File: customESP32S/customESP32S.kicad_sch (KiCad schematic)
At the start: 0 parts

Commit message: finished two USB micro connections with their protection circuit
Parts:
- added C1, C2: 10uF/25V, symbol Device:C_Small
- added D1, D8: 1N5819, Diode_THT:D_DO-41_SOD81_P10.16mm_Horizontal, symbol Diode:1N5819
- added D2, D3, D4, D5, D6, D7: SD05_SOD323, Diode_SMD:D_SOD-323, symbol Diode:SD05_SOD323
- added J1, J2: USB_B_Micro, symbol Connector:USB_B_Micro
- added U1: RT9193-33GB, RT9193-33GB:SOT94P279X129-5N, symbol RT9193-33GB:RT9193-33GB
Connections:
- new net GND: C1.1, C2.1, D2.1 (A1), D3.1 (A1), D4.1 (A1), D5.1 (A1), D6.1 (A1), D7.1 (A1), J1.5 (GND), J1.6 (Shield), J2.5 (GND), J2.6 (Shield)
- new net GPIO19: D2.2 (A2), J1.2 (D-)
- new net GPIO20: D3.2 (A2), J1.3 (D+)
- new net USB_DN: D5.2 (A2), J2.2 (D-)
- new net USB_DP: D6.2 (A2), J2.3 (D+)
- new net VBUS: D7.2 (A2), D8.2 (A), J2.1 (VBUS)
- new net VBUSB: D1.2 (A), D4.2 (A2), J1.1 (VBUS)
- new net VCC_5V: C1.2, C2.2, D1.1 (K), D8.1 (K)
- no-connect marks 0 -> 2
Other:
- note added: "ESP USB"
- note added: "USB to UART"

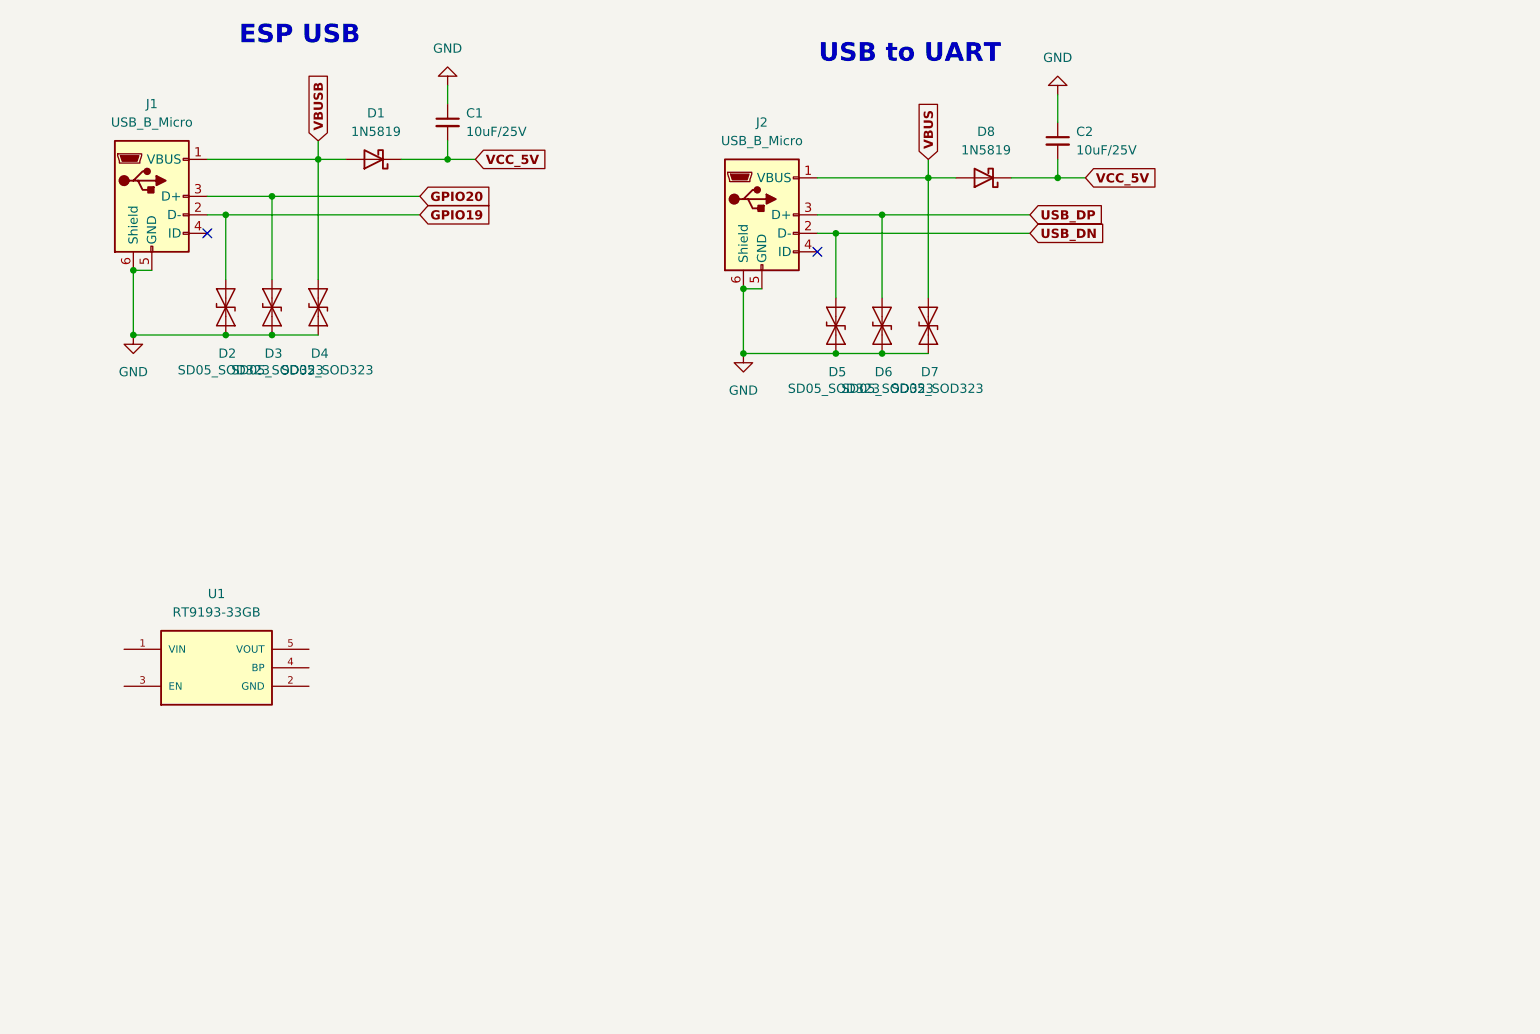
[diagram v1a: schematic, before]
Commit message: added AMS1117-3.3v LDO schematic design
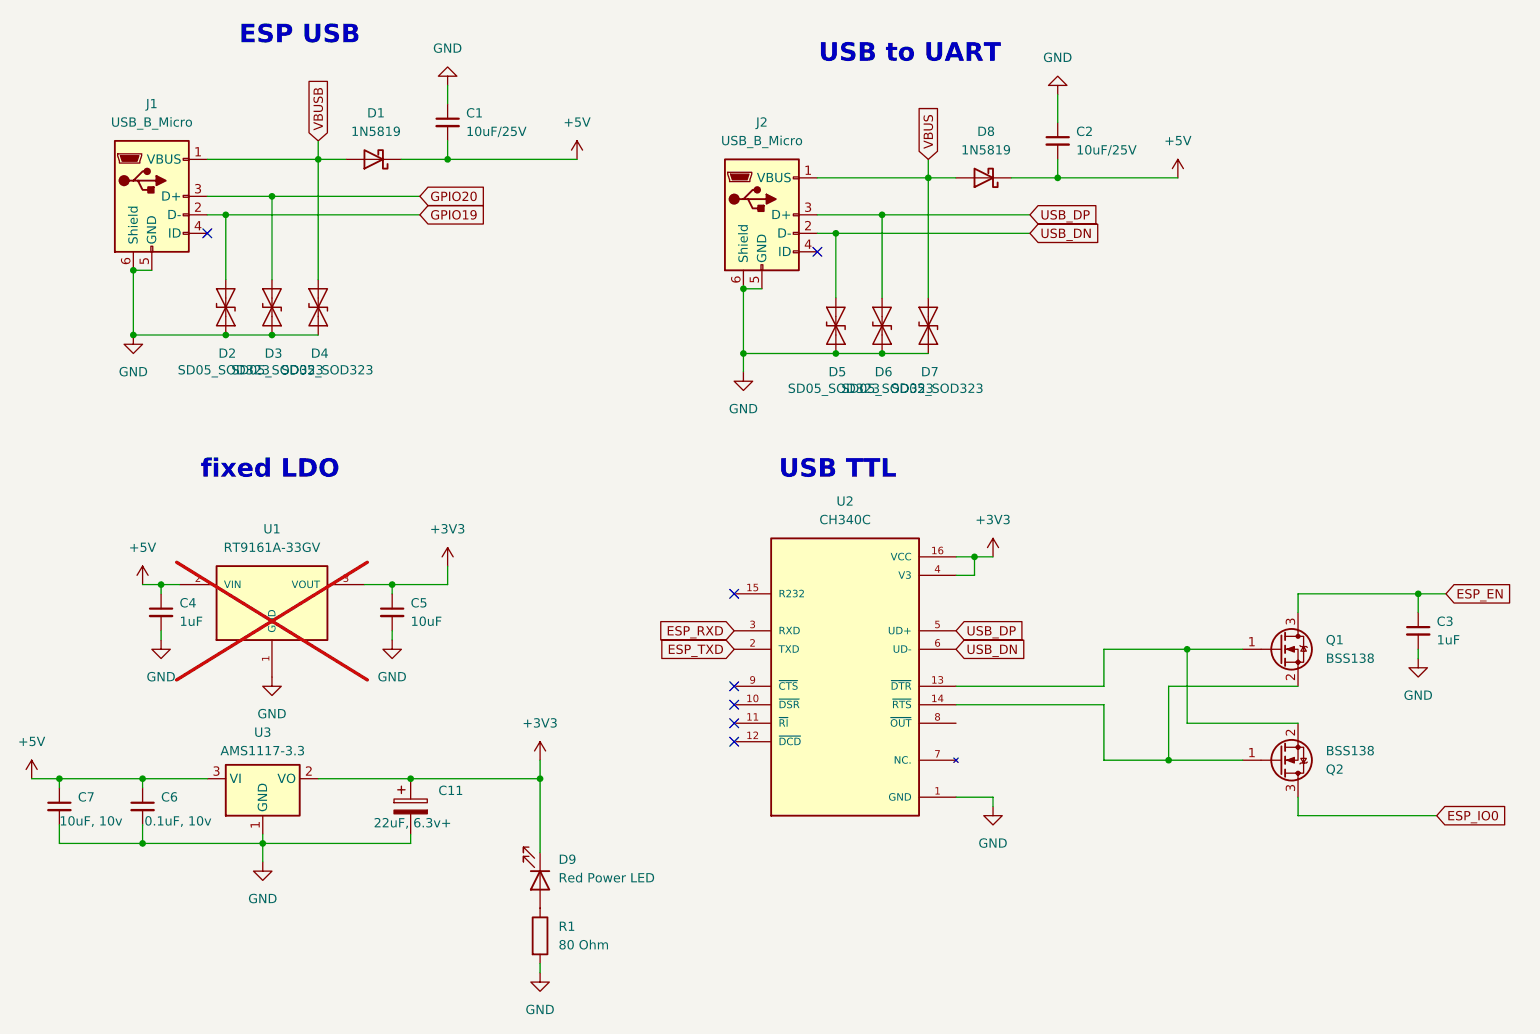
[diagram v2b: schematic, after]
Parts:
- removed U1: RT9193-33GB, RT9193-33GB:SOT94P279X129-5N, symbol RT9193-33GB:RT9193-33GB
- added C11: 22uF, 6.3v+, symbol Device:C_Polarized
- added C3, C4: 1uF, symbol Device:C_Small
- added C5: 10uF, symbol Device:C_Small
- added C6: 0.1uF, 10v, symbol Device:C_Small
- added C7: 10uF, 10v, symbol Device:C_Small
- added D9: Red Power LED, symbol Device:LED
- added Q1, Q2: BSS138, Package_TO_SOT_SMD:SOT-23, symbol Transistor_FET:BSS138
- added R1: 80 Ohm, symbol Device:R
- added U1: RT9161A-33GV, Package_TO_SOT_SMD:SOT-23-3, symbol RT9161A-33GV:RT9161A-33GV
- added U2: CH340C, CH340C:SOIC127P600X180-16N, symbol CH340C:CH340C
- added U3: AMS1117-3.3, Package_TO_SOT_SMD:SOT-223-3_TabPin2, symbol Regulator_Linear:AMS1117-3.3
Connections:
- net GND: now also C11.2, C3.2, C4.2, C5.2, C6.2, C7.2, R1.2, U1.1 (GND), U2.1 (GND), U3.1 (GND)
- net USB_DN: now also U2.6 (UD-)
- net USB_DP: now also U2.5 (UD+)
- net VCC_5V renamed +5V
- net +5V: now also C4.1, C6.1, C7.1, U1.2 (VIN), U3.3 (VI)
- new net: Q1.1 (G), Q2.2 (S), U2.13 (~{DTR})
- new net: Q1.2 (S), Q2.1 (G), U2.14 (~{RTS})
- new net: D9.2 (A), R1.1
- new net +3V3: C11.1, C5.1, D9.1 (K), U1.3 (VOUT), U2.16 (VCC), U2.4 (V3), U3.2 (VO)
- new net ESP_EN: C3.1, Q1.3 (D)
- new net ESP_IO0: Q2.3 (D)
- new net ESP_RXD: U2.3 (RXD)
- new net ESP_TXD: U2.2 (TXD)
- no-connect marks 2 -> 7
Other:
- note added: "USB TTL"
- note added: "fixed LDO"
